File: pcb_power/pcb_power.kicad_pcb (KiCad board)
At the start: 2 copper layers, 32.7 x 27.8 mm, 25 parts, among them J1 Pwr_jmp, J2 CPU_jmp, SW1 SW_SPDT, SW2 SW_SPST, SW3 SW_SPST, SW4 SW_SPST, U1 RP402N331F, U2 LoRa-E5, U3 IN-S128TATRGB

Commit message: Changes
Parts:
- added AE1: Antenna_Shield, Connector_Coaxial:U.FL_Molex_MCRF_73412-0110_Vertical, F.Cu at (145.2, 99.6)
- added BT1: Battery, Connector_PinHeader_2.54mm:PinHeader_1x02_P2.54mm_Horizontal, F.Cu at (151.8, 72.3)
- added C5: 10u, Capacitor_SMD:C_0805_2012Metric, F.Cu at (144.5, 93.7)
- added CR1: STTS75M2F, STTS75M2F:STTS75M2F, F.Cu at (147.1, 89.2)
- added R5: 10k, Resistor_SMD:R_0805_2012Metric, F.Cu at (152.7, 90.9)
- added R6: 10k, Resistor_SMD:R_0805_2012Metric, F.Cu at (152.7, 88.9)
- added R7: 10k, Resistor_SMD:R_0805_2012Metric, F.Cu at (152.7, 86.9)
- J3: renamed from 3V3 / TX / RX / GND
- J4: renamed from SWCLK / SWDIO / GND / 3V3
- moved C4 13.9 mm to (168.1, 100.8), turned to 90 degrees
- moved J4 9.50 mm to (170.2, 88.6), turned to 90 degrees
- moved J2 7.92 mm to (168.8, 96.6)
- moved JP1 6.00 mm to (177.8, 93.3), turned to 180 degrees
- moved J1 2.70 mm to (175.1, 96.6), turned to 90 degrees
- moved JP2 1.65 mm to (174.4, 93.3)
- moved SW3 0.87 mm to (149.8, 100.1)
- moved J3 0.54 mm to (158.6, 88.6)
- moved SW4 0.44 mm to (152.4, 107.8)
- moved SW2 0.43 mm to (152.4, 112.0)
- moved D1 0.36 mm to (158.7, 112.4)
- moved U3 0.35 mm to (165.7, 114.0)
- moved SW1 0.25 mm to (172.1, 112.4)
- moved R1 0.23 mm to (164.8, 109.0)
- moved R2 0.23 mm to (162.8, 109.0)
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- renumbered Vreg-3V3 to JP1, 3V3-Vcc to JP2
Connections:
- J4 pad 1: +3V3 -> GND
- J4 pad 2: GND -> +3V3
- SW1 pad : GND -> (no net)
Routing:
- net GND: track 33.4 -> 0.45 mm, vias 1 -> 0
- net PB15/SCL: track 0.00 -> 26.3 mm, vias 0 -> 2
- net PA15/SDA: track 0.00 -> 25.9 mm, vias 0 -> 2
- net +3V3: track 45.4 -> 62.8 mm
- net Vcc: track 27.4 -> 15.0 mm, vias 1 -> 0
- net SWDIO/PA13: track 13.4 -> 25.1 mm
- net SWCLK/PA14: track 13.3 -> 24.3 mm
- net RFIO: track 0.00 -> 9.98 mm
- net BOOT/PB13: track 0.00 -> 9.87 mm
- net RST: track 22.8 -> 19.7 mm
- net Net-(CR1-Pad3): track 0.00 -> 2.90 mm
- added copper zone on B.Cu, net GND
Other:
- board size 32.7 x 27.8 mm -> 38 x 28.7 mm
- board text added: "CLK"
- board text added: "CPU Jump"
- board text added: "DIO"
- board text added: "RX"
- board text added: "TX"
- board text added: "VReg Jump"

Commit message: Lili rework 2
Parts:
- removed the J2 at (177.4, 105.6)
- added REF**: MountingHole_2.2mm_M2, MountingHole:MountingHole_2.2mm_M2, F.Cu at (177.7, 88.3)
- added REF**: MountingHole_2.2mm_M2, MountingHole:MountingHole_2.2mm_M2, F.Cu at (144.5, 88.1)
- added REF**: MountingHole_2.2mm_M2, MountingHole:MountingHole_2.2mm_M2, F.Cu at (144.8, 111.5)
- BT1: moved to B.Cu
- moved BT1 44.3 mm to (177.9, 108.1)
- moved R7 14.0 mm to (146.4, 99.4), turned to 90 degrees
- moved AE1 12.4 mm to (149.9, 88.1), turned to 0 degrees
- moved R6 10.8 mm to (150.2, 99.4), turned to 90 degrees
- moved C4 9.70 mm to (167.2, 91.2), turned to 180 degrees
- moved R5 9.54 mm to (148.3, 99.4), turned to 90 degrees
- moved SW3 8.41 mm to (152.4, 108.1), turned to 180 degrees
- moved SW4 6.71 mm to (147.1, 103.8)
- moved C5 5.74 mm to (144.0, 99.4)
- moved CR1 5.21 mm to (147.2, 94.4)
- moved J3 4.46 mm to (154.2, 88.4)
- moved J4 4.46 mm to (165.7, 88.4)
- moved J2 3.53 mm to (170.9, 93.9), turned to 0 degrees
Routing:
- net +3V3: track 62.8 -> 31.2 mm
- net SWCLK/PA14: track 24.3 -> 2.53 mm
- net SWDIO/PA13: track 25.1 -> 3.44 mm
- net PA15/SDA: track 25.9 -> 8.25 mm, vias 2 -> 1
- net PB15/SCL: track 26.3 -> 11.1 mm, vias 2 -> 1
- net RFIO: track 9.98 -> 0.00 mm
- net BOOT/PB13: track 9.87 -> 0.91 mm
- net Vcc: track 15.0 -> 7.35 mm
- net LED_STATUS: track 16.4 -> 11.6 mm
- net RX/PB7: track 4.28 -> 0.00 mm
- net PA0/BUTTON: track 3.93 -> 0.00 mm
- net TX/PB6: track 3.75 -> 0.00 mm
- net Net-(CR1-Pad3): track 2.90 -> 6.56 mm
- net RST: track 19.7 -> 22.4 mm
- net GND: vias 0 -> 16

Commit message: DRC Fixes, etc
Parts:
- added J5: Pins Header, Connector_PinHeader_2.54mm:PinHeader_1x04_P2.54mm_Vertical_SMD_Pin1Left, B.Cu at (131.6, 40.1)
- added JP3: Pwr_jmp, Jumper:SolderJumper-2_P1.3mm_Bridged2Bar_Pad1.0x1.5mm, B.Cu at (138.7, 41.9)
- locked: renamed from SW1; value SW_SPDT -> locked
- locked: renamed from C2; value 10u -> locked
- moved SW2 76.5 mm to (126.1, 40.1), turned to -90 degrees
- moved SW3 71.4 mm to (130.3, 40.1), turned to -90 degrees
- moved JP2 66.2 mm to (155.3, 30.0)
- moved REF** 65.9 mm to (126.4, 24.8)
- moved REF** 65.9 mm to (126.4, 48.3)
- moved J3 65.5 mm to (137.9, 24.9)
- moved JP1 65.4 mm to (161.5, 30.0)
- moved REF** 65.3 mm to (162.6, 24.8)
- moved C3 65.2 mm to (161.6, 38.5)
- moved J1 65.2 mm to (160.1, 33.1)
- moved L1 65.2 mm to (158.9, 42.3)
- moved TP1 65.2 mm to (153.8, 42.5)
- moved U1 65.2 mm to (158.5, 38.8)
- moved U3 65.2 mm to (150.7, 50.5)
- moved BT1 65.2 mm to (162.9, 44.6)
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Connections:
- J4 pad 2: +3V3 -> RST
- U2 pad 18: unconnected-(U2-Pad18) -> PA3
- U2 pad 19: unconnected-(U2-Pad19) -> PA2
- U2 pad 20: unconnected-(U2-Pad20) -> PB10
- U2 pad 21: unconnected-(U2-Pad21) -> PA9
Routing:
- net +3V3: track 31.2 -> 97.1 mm, vias 1 -> 3
- net PA15/SDA: track 8.25 -> 38.1 mm, vias 1 -> 2
- net PB15/SCL: track 11.1 -> 34.4 mm, vias 1 -> 2
- net BOOT/PB13: track 0.91 -> 17.5 mm
- net RST: track 22.4 -> 37.6 mm, vias 2 -> 1
- net PA0/BUTTON: track 0.00 -> 13.4 mm
- net LED_STATUS: track 11.6 -> 24.4 mm
- net PA3: track 0.00 -> 12.1 mm, vias 0 -> 1
- net PB10: track 0.00 -> 9.94 mm, vias 0 -> 1
- net SWDIO/PA13: track 3.44 -> 12.9 mm, vias 1 -> 0
- net SWCLK/PA14: track 2.53 -> 11.8 mm, vias 1 -> 0
- net PA9: track 0.00 -> 9.01 mm, vias 0 -> 1
- net TX/PB6: track 0.00 -> 8.10 mm
- net PA2: track 0.00 -> 6.59 mm, vias 0 -> 1
- net RX/PB7: track 0.00 -> 5.91 mm
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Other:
- board size 38 x 28.7 mm -> 41.3 x 28.6 mm
- board text added: "A3"
- board text added: "A9"
- board text added: "B10"
- board text added: "RST"

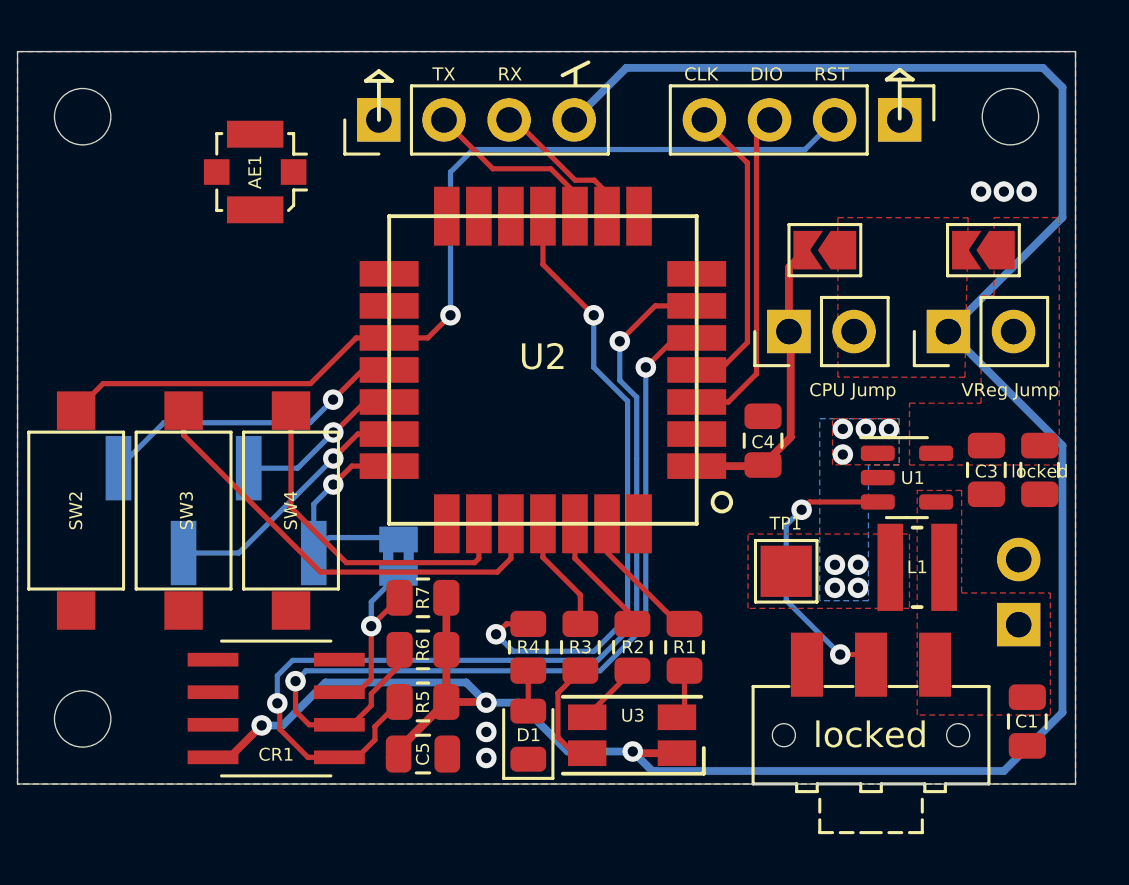
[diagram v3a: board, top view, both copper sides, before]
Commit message: Final ZP changes before antenna rework and cosmetix
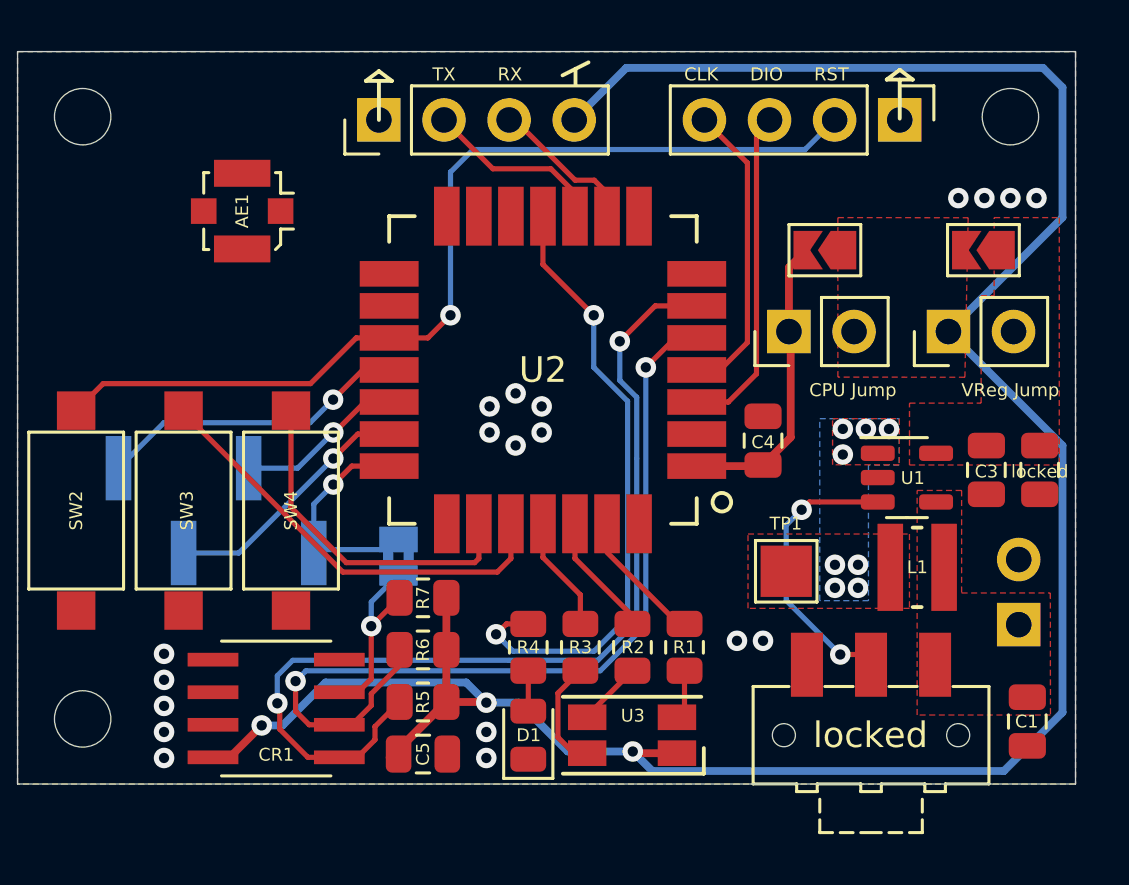
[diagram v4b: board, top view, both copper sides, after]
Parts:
- moved AE1 1.61 mm to (132.6, 28.4)
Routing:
- net BOOT/PB13: track 17.5 -> 17.0 mm
- net GND: vias 5 -> 19
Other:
- board text added: "0"
- board text added: "Adorable AyeAye"
- board text added: "Lora Temp Sensor"
- board text added: "Rev"

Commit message: Add files via upload
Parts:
- added C6: C, Capacitor_SMD:C_0603_1608Metric_Pad1.08x0.95mm_HandSolder, F.Cu at (133.5, 31.9)
- added C7: C, Capacitor_SMD:C_0603_1608Metric_Pad1.08x0.95mm_HandSolder, F.Cu at (128.4, 31.9)
- added R8: R, Resistor_SMD:R_0603_1608Metric_Pad0.98x0.95mm_HandSolder, F.Cu at (130.9, 31.0)
- added R9: R, Resistor_SMD:R_0603_1608Metric_Pad0.98x0.95mm_HandSolder, F.Cu at (126.6, 30.0)
- JP3: value Pwr_jmp -> OSINT_Jmp
- moved AE1 6.91 mm to (126.6, 25.0), turned to 0 degrees
- moved REF** 5.75 mm to (132.1, 25.4)
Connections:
- AE1 pad 1: RFIO -> Net-(AE1-Pad1)
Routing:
- net RFIO: track 0.00 -> 6.55 mm
- net Net-(C7-Pad1): track 0.00 -> 3.24 mm
- net Net-(AE1-Pad1): track 0.00 -> 2.60 mm
- net RST: track 37.6 -> 40.2 mm
- net (no net): vias 0 -> 17
